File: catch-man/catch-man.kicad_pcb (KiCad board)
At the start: 2 copper layers, 108.8 x 118.5 mm, 24 parts, among them Q1 2N3904, SW1 SW_Push_45deg, SW2 SW_SPDT, U1 STC8G1K08A-36I-DFN8

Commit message: catch-man: v1
Finished layout, centered parts
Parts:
- added C1: 0.1u, Capacitor_THT:C_Disc_D3.0mm_W1.6mm_P2.50mm, F.Cu at (149.8, 142.2)
- LS1: value Speaker -> 9024 Passive Buzzer; footprint Buzzer_Beeper:Buzzer_12x9.5RM7.6 -> Buzzer_Beeper:MagneticBuzzer_PUI_AT-0927-TT-6-R
- Q1: value 2N3904 -> 2N2222; footprint Package_TO_SOT_THT:TO-92_Inline -> Package_TO_SOT_THT:TO-18-3
- SW2: value SW_SPDT -> POWER
- U1: value STC8G1K08A-36I-DFN8 -> STC8G1K08A-36I-DIP8
- moved R1 31.8 mm to (162.6, 138.4), turned to 90 degrees
- moved R4 24.9 mm to (157.5, 138.4), turned to 90 degrees
- moved D5 21.4 mm to (154.3, 158.7)
- moved D9 21.0 mm to (163.2, 158.7)
- moved D6 20.3 mm to (145.4, 156.2), turned to -90 degrees
- moved R2 19.1 mm to (134.6, 138.4), turned to 90 degrees
- moved D11 16.4 mm to (149.9, 121.9), turned to 180 degrees
- moved SW2 16.0 mm to (132.1, 154.9), turned to -90 degrees
- moved LS1 16.0 mm to (141.7, 83.8), turned to 180 degrees
- moved D8 15.5 mm to (129.5, 121.9)
- moved D3 15.3 mm to (172.7, 97.8), turned to 180 degrees
- moved BT1 14.7 mm to (116.5, 145.9)
- moved R3 14.5 mm to (139.7, 138.4), turned to 90 degrees
- moved D4 14.1 mm to (158.7, 109.2)
- moved R5 14.0 mm to (126.9, 79.9)
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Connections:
- net Net-(SW2-A) renamed /VCC
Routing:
- net /VCC: track 0.00 -> 179.6 mm
- net GND: track 0.00 -> 177.3 mm
- net Net-(D1-A): track 0.00 -> 154.8 mm, vias 0 -> 1
- net Net-(D10-A): track 0.00 -> 140.8 mm
- net Net-(U1-P3.1): track 0.00 -> 132.3 mm
- net Net-(D1-K): track 0.00 -> 113.4 mm
- net Net-(D11-K): track 0.00 -> 105.2 mm
- net Net-(U1-P3.0): track 0.00 -> 31.4 mm
- net Net-(Q1-B): track 0.00 -> 27.0 mm
- net Net-(BT1-+): track 0.00 -> 17.9 mm
- net Net-(Q1-C): track 0.00 -> 17.6 mm
- net Net-(U1-P3.3): track 0.00 -> 13.3 mm
- net Net-(U1-P5.4): track 0.00 -> 13.3 mm
- net Net-(U1-P3.2): track 0.00 -> 7.19 mm
- net Net-(U1-P5.5): track 0.00 -> 6.13 mm
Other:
- board size 108.8 x 118.5 mm -> 108.2 x 119.4 mm
- board text added: "OFF"
- board text added: "ON"

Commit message: catch-man v1: done, ordered
Add 2nd footprint for speaker - not sure which one will work
best

Add README.md
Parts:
- added LS2: 15mm / 10mm buzzer, Buzzer_Beeper:Buzzer_D14mm_H7mm_P10mm, F.Cu at (144.8, 83.8)
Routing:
- net Net-(Q1-C): track 17.6 -> 20.6 mm
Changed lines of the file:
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@@
+		)
+	)
+	(footprint "Buzzer_Beeper:Buzzer_D14mm_H7mm_P10mm"
+		(layer "F.Cu")
+		(at 144.751152 83.815696 180)
+		(descr "Generic Buzzer, D14mm height 7mm with pitch 10mm")
+		(tags "buzzer")
+		(property "Reference" "LS2"
+			(at 5.16 -8.23 0)
+			(layer "F.SilkS")
+			(hide yes)
+			(effects
+				(font
+					(size 1 1)
+					(thickness 0.15)
+				)
+			)
+		)
+		(property "Value" "15mm / 10mm buzzer"
+			(at 4.69 8.41 0)
+			(layer "F.Fab")
+			(hide yes)
+			(effects
+				(font
+					(size 1 1)
+					(thickness 0.15)
+				)
+			)
+		)
+		(property "Datasheet" "~"
+			(at 0 0 180)
+			(unlocked yes)
+			(layer "F.Fab")
+			(hide yes)
+			(effects
+				(font
+					(size 1.27 1.27)
+					(thickness 0.15)
+				)
+			)
+		)
+		(property "Description" "Speaker"
+			(at 0 0 180)
+			(unlocked yes)
+			(layer "F.Fab")
+			(hide yes)
+			(effects
+				(font
+					(size 1.27 1.27)
+					(thickness 0.15)
+				)
+			)
+		)
+		(sheetname "/")
+		(sheetfile "catch-man.kicad_sch")
+		(attr through_hole)
+		(fp_circle
+			(center 5 0)
+			(end 12.1 0)
+			(stroke
+				(width 0.12)
+				(type solid)
+			)
+			(fill no)
+			(layer "F.SilkS")
+		)
+		(fp_circle
+			(center 5 0)
+			(end 12.25 0)
+			(stroke
+				(width 0.05)
+				(type solid)
+			)
+			(fill no)
+			(layer "F.CrtYd")
+		)
+		(fp_circle
+			(center 5 0)
+			(end 12 0)
+			(stroke
+				(width 0.1)
+				(type solid)
+			)
+			(fill no)
+			(layer "F.Fab")
+		)
+		(fp_circle
+			(center 5 0)
+			(end 6 0)
+			(stroke
+				(width 0.1)
+				(type solid)
+			)
+			(fill no)
+			(layer "F.Fab")
+		)
+		(fp_text user "+"
+			(at -0.01 -2.54 0)
+			(layer "F.SilkS")
+			(effects
+				(font
+					(size 1 1)
+					(thickness 0.15)
+				)
+			)
+		)
+		(fp_text user "+"
+			(at -0.01 -2.54 0)
+			(layer "F.Fab")
+			(effects
+				(font
+					(size 1 1)
+					(thickness 0.15)
+				)
+			)
+		)
+		(fp_text user "${REFERENCE}"
+			(at 5.32 2.27 0)
+			(layer "F.Fab")
+			(effects
+				(font
+					(size 1 1)
+					(thickness 0.15)
+				)
+			)
+		)
+		(pad "1" thru_hole rect
+			(at 0 0 180)
+			(size 2 2)
+			(drill 1)
+			(layers "*.Cu" "*.Mask")
+			(remove_unused_layers no)
+			(net 15 "/VCC")
+			(pinfunction "1")
+			(pintype "input")
+		)
+		(pad "2" thru_hole circle
+			(at 10 0 180)
+			(size 2 2)
+			(drill 1)
+			(layers "*.Cu" "*.Mask")
+			(remove_unused_layers no)
+			(net 8 "Net-(Q1-C)")
+			(pinfunction "2")
+			(pintype "input")
+		)
+		(embedded_fonts no)
+		(model "${KICAD9_3DMODEL_DIR}/Buzzer_Beeper.3dshapes/Buzzer_D14mm_H7mm_P10mm.step"
+			(offset
+				(xyz 0 0 0)
+			)
+			(scale
+				(xyz 1 1 1)
+			)
+			(rotate
+				(xyz 0 0 0)
+			)
 		)
 	)
@@
 	)
 	(segment
+		(start 134.755456 83.82)
+		(end 134.751152 83.815696)
+		(width 0.508)
+		(layer "B.Cu")
+		(net 8)
+	)
+	(segment
 		(start 140.245 86.36)
 		(end 137.705 83.82)
@@
 	)
 	(segment
+		(start 137.705 83.82)
+		(end 134.755456 83.82)
+		(width 0.508)
+		(layer "B.Cu")
+		(net 8)
+	)
+	(segment
 		(start 152.405 86.36)
 		(end 140.245 86.36)
@@
 	)
 	(segment
+		(start 167.645 80.01)
+		(end 148.595 80.01)
+		(width 0.508)
+		(layer "B.Cu")
+		(net 15)
+	)
+	(segment
+		(start 151.135 146.05)
+		(end 184.155 146.05)
+		(width 0.508)
+		(layer "B.Cu")
+		(net 15)
+	)
+	(segment
+		(start 184.155 146.05)
+		(end 185.425 144.78)
+		(width 0.508)
+		(layer "B.Cu")
+		(net 15)
+	)
+	(segment
+		(start 149.826138 142.211958)
+		(end 149.826138 144.741138)
+		(width 0.508)
+		(layer "B.Cu")
+		(net 15)
+	)
+	(segment
 		(start 149.826138 144.741138)
 		(end 151.135 146.05)
@@
 	)
 	(segment
-		(start 184.155 146.05)
-		(end 185.425 144.78)
+		(start 144.785 83.82)
+		(end 141.705 83.82)
 		(width 0.508)
 		(layer "B.Cu")
@@
 	)
 	(segment
-		(start 143.430676 83.82)
-		(end 141.705 83.82)
-		(width 0.508)
-		(layer "B.Cu")
-		(net 15)
-	)
-	(segment
-		(start 147.240676 80.01)
-		(end 143.430676 83.82)
-		(width 0.508)
-		(layer "B.Cu")
-		(net 15)
-	)
-	(segment
-		(start 149.826138 142.211958)
-		(end 149.826138 144.741138)
+		(start 148.595 80.01)
+		(end 144.785 83.82)
 		(width 0.508)
 		(layer "B.Cu")
@@
 		(width 0.508)
 		(layer "B.Cu")
-		(net 15)
-	)
-	(segment
-		(start 167.645 80.01)
-		(end 147.240676 80.01)
-		(width 0.508)
-		(layer "B.Cu")
-		(net 15)
-	)
-	(segment
-		(start 151.135 146.05)
-		(end 184.155 146.05)
-		(width 0.508)
-		(layer "B.Cu")

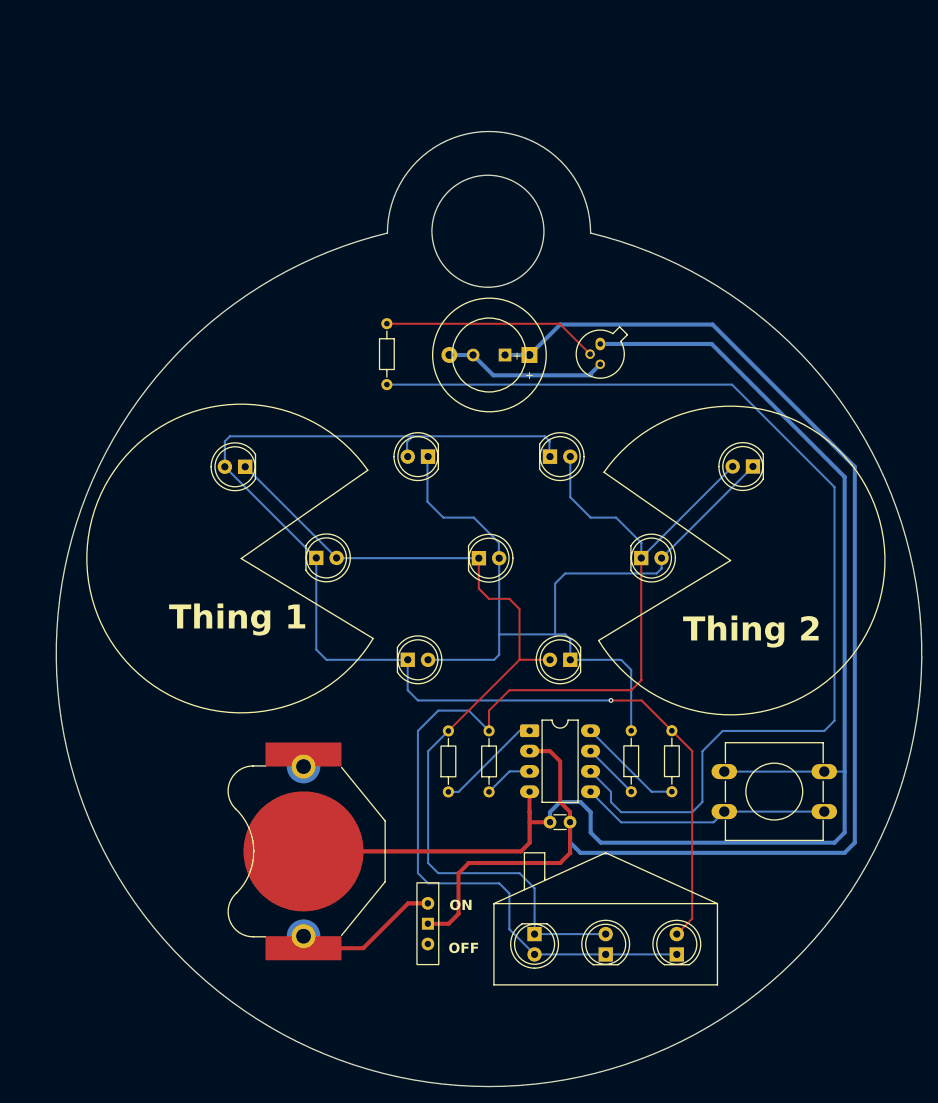
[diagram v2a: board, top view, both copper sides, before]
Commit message: catch-man: start on board redesign
To keep things simple, don't change connection pinout, duplicate
manual changes on existing protype

The "catch-man" caption is not big enough yet, we'll want to move it
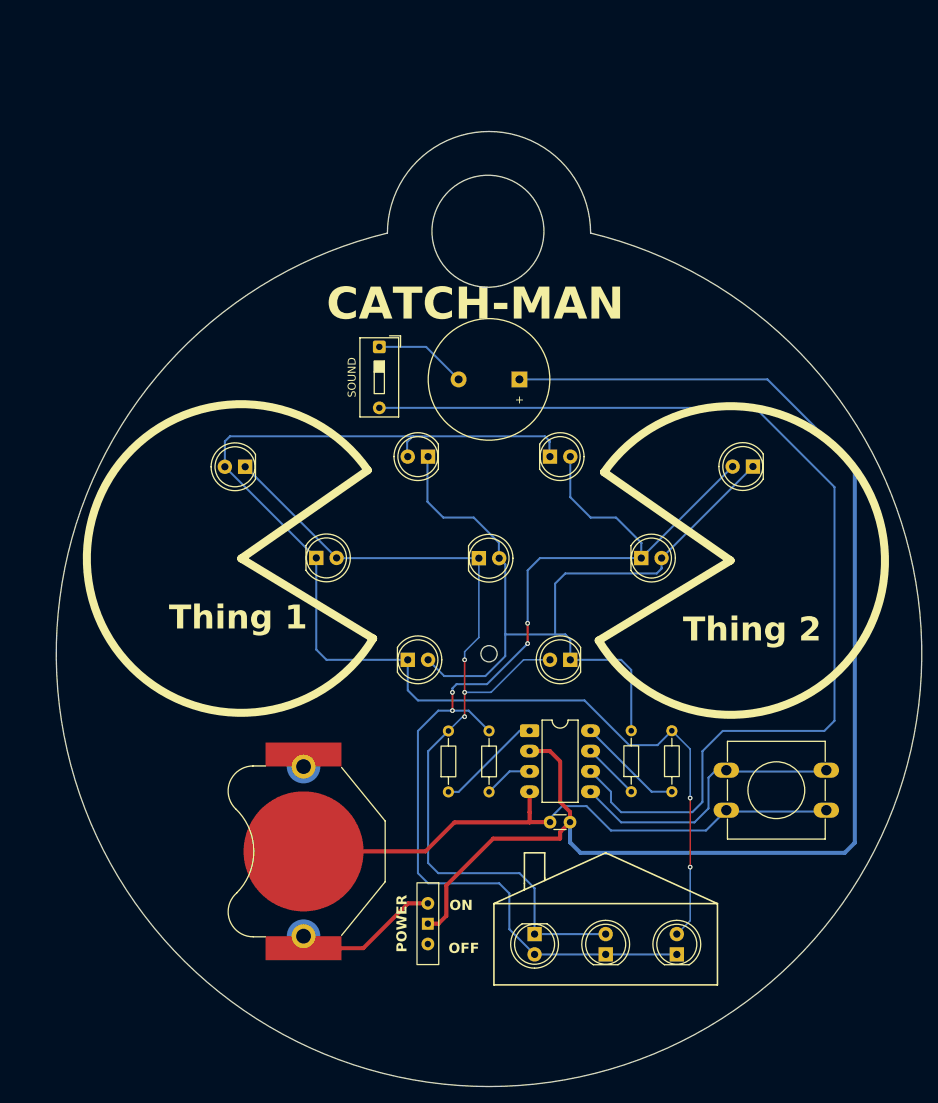
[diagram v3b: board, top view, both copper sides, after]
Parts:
- removed LS2: 15mm / 10mm buzzer, Buzzer_Beeper:Buzzer_D14mm_H7mm_P10mm
- removed Q1: 2N2222, Package_TO_SOT_THT:TO-18-3
- removed R5: 120, Resistor_THT:R_Axial_DIN0204_L3.6mm_D1.6mm_P7.62mm_Horizontal
- added SW3: SOUND, Button_Switch_THT:SW_DIP_SPSTx01_Slide_9.78x4.72mm_W7.62mm_P2.54mm, F.Cu at (126.0, 82.8)
- LS1: value 9024 Passive Buzzer -> 1407 Passive Piezo; footprint Buzzer_Beeper:MagneticBuzzer_PUI_AT-0927-TT-6-R -> Buzzer_Beeper:Buzzer_15x7.5RM7.6
- moved SW1 13.6 mm to (181.9, 140.7), turned to 180 degrees
- moved LS1 3.54 mm to (143.5, 86.9)
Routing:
- net GND: track 177.3 -> 74.1 mm
- net Net-(Q1-B): track 27.0 -> 0.00 mm
- net Net-(SW3-A): track 20.6 -> 11.6 mm
- net /VCC: track 179.6 -> 170.8 mm
- net Net-(U1-P3.0): track 31.4 -> 36.0 mm
- net Net-(D1-K): track 113.4 -> 116.4 mm, vias 0 -> 3
- net Net-(D11-K): track 105.2 -> 107.3 mm
- net Net-(D1-A): track 154.8 -> 156.1 mm, vias 1 -> 2
- net Net-(D10-A): track 140.8 -> 140.9 mm, vias 0 -> 4
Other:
- outline, holes or cut-outs redrawn
- board text added: "CATCH-MAN"
- board text added: "Catch-man v1.1 designed by theamk"
- board text added: "POWER"
- board text removed: "Catch-man v1.0 designed by theamk"

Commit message: catch-man: board v1.1
Moved speaker to the bottom, added large text on top.
Re-routed bottom section.

Also fixed CR2032-THT-retainer part so it does not throw
as much DRC errors.
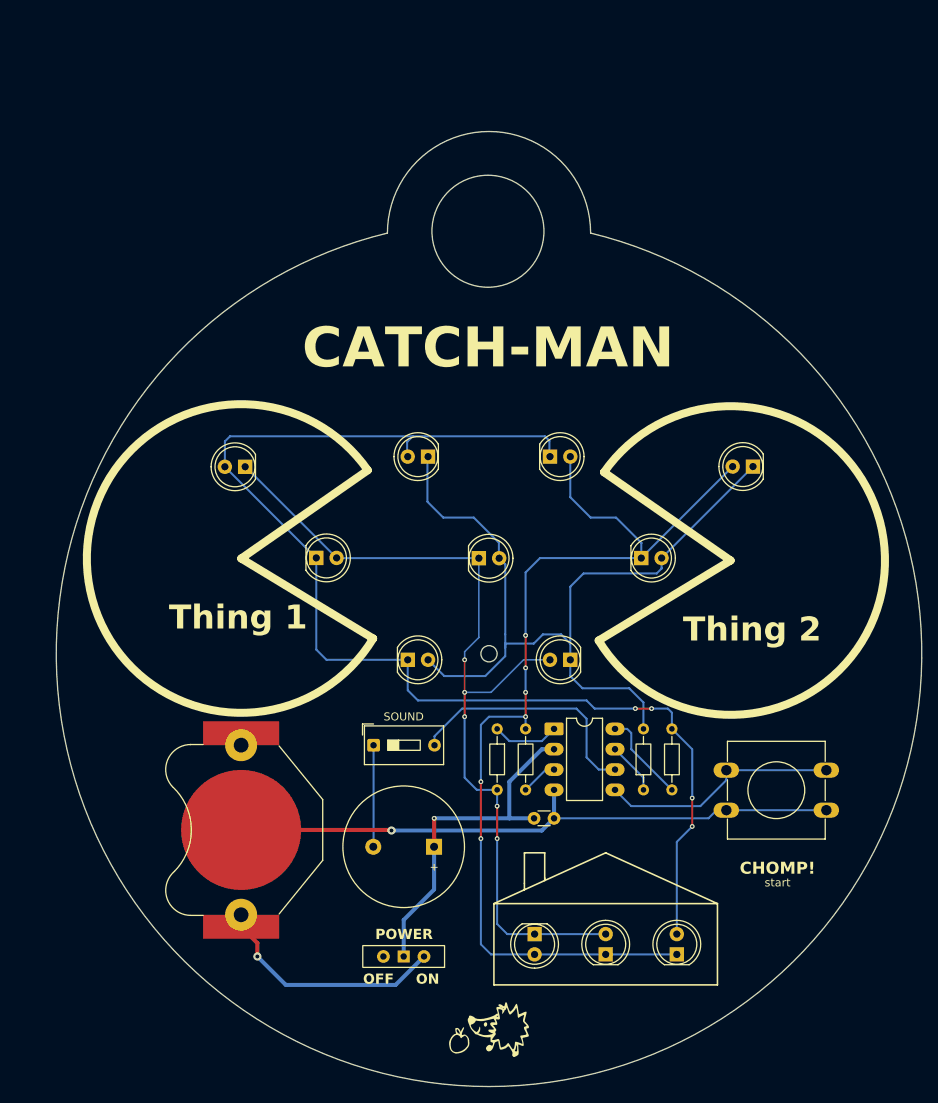
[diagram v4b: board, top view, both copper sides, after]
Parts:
- added G***: LOGO, LOGO, F.Cu at (139.7, 168.1)
- moved LS1 59.4 mm to (132.8, 145.3)
- moved SW3 49.8 mm to (125.3, 132.6), turned to 0 degrees
- moved R2 9.95 mm to (140.7, 130.6), turned to -90 degrees
- moved BT1 8.25 mm to (108.7, 143.2)
- moved SW2 5.09 mm to (129.0, 159.0), turned to 180 degrees
- moved R3 4.57 mm to (144.3, 138.2)
- moved C1 4.52 mm to (145.3, 141.7), turned to 0 degrees
- moved U1 3.06 mm to (147.8, 130.6)
- moved R4 1.54 mm to (159.0, 138.2)
- moved R1 0.23 mm to (162.6, 138.2)
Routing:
- net /VCC: track 170.8 -> 43.2 mm, vias 0 -> 1
- net Net-(SW3-B): track 132.0 -> 31.1 mm
- net Net-(D10-A): track 140.9 -> 127.7 mm, vias 4 -> 6
- net Net-(BT1-+): track 17.9 -> 28.3 mm, vias 0 -> 1
- net Net-(D1-K): track 116.4 -> 110.0 mm, vias 3 -> 5
- net Net-(U1-P3.0): track 36.0 -> 29.8 mm
- net Net-(U1-P5.4): track 13.3 -> 8.37 mm
- net GND: track 74.1 -> 77.8 mm, vias 0 -> 1
- net Net-(U1-P3.3): track 13.3 -> 11.5 mm
- net Net-(U1-P5.5): track 6.13 -> 4.61 mm
- net Net-(SW3-A): track 11.6 -> 12.7 mm
- net Net-(U1-P3.2): track 7.19 -> 6.55 mm
- net Net-(D1-A): vias 2 -> 4
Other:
- board text added: "CHOMP!"
- board text added: "start"

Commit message: catch-man: board update
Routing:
- net Net-(BT1-+): track 28.3 -> 34.4 mm
